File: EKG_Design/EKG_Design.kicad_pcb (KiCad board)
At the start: 2 copper layers, 40.7 x 23.2 mm, 55 parts, among them IC101 OPA2156IDGKR, IC102 OPA2156IDGKR, IC103 OPA2156IDGKR, IC104 INA826AIDR_/_SOIC8, J100 Conn_01x02_Pin, J101 Conn_01x02_Pin, J102 Conn_01x02_Pin, J103 Conn_01x02_Pin, J104 Conn_01x03_Pin, Q200 BC848C

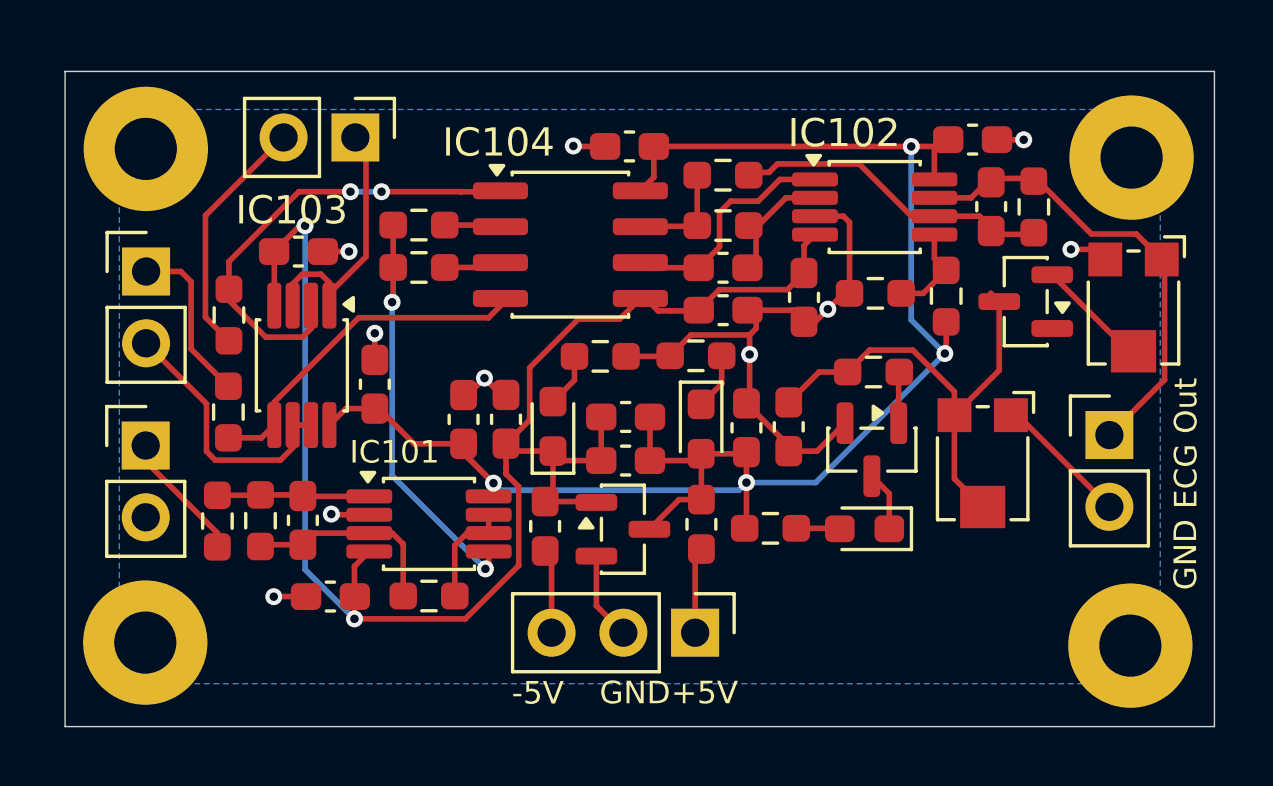
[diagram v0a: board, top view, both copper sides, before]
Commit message: Added GND zone to front of the board
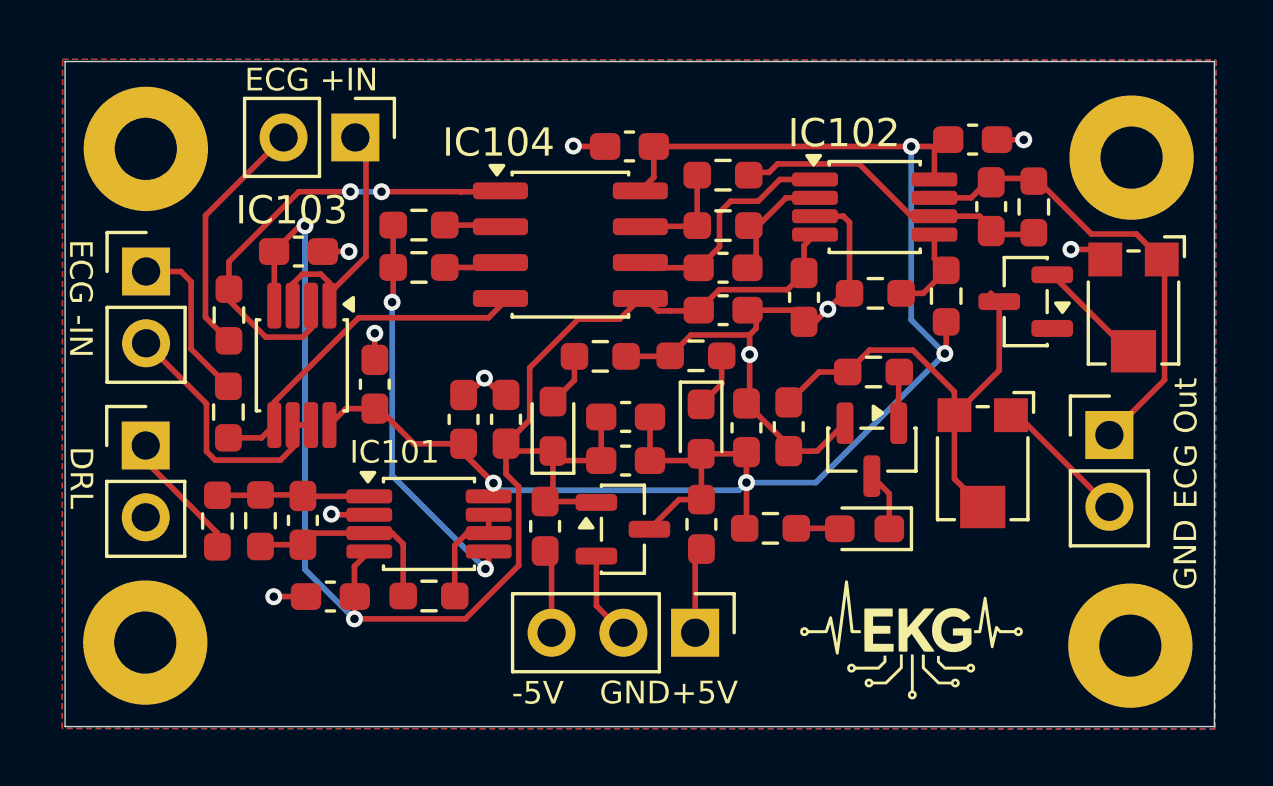
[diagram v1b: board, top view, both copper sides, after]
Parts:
- added G***: LOGO, logos:Logo, F.Cu at (122.0, 87.5)
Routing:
- added copper zone on F.Cu, net GND
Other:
- board size 40.7 x 23.2 mm -> 40.7 x 23.5 mm
- board text added: "DRL"
- board text added: "ECG +IN"
- board text added: "ECG -IN"

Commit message: added ibom and jobsets
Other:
- board text added: "T. Brown M. Mousa"
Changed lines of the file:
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@@
 			(drillshape 1)
 			(scaleselection 1)
-			(outputdirectory "")
+			(outputdirectory "Gerber")
 		)
 	)
@@
 		(sheetname "/ECG-PulseDetection/")
 		(sheetfile "ECG-PulseDetection.kicad_sch")
-		(units
-			(unit
-				(name "A")
-				(pins "1" "2")
-			)
-		)
 		(attr smd)
 		(duplicate_pad_numbers_are_jumpers no)
@@
 			(layer "F.CrtYd")
 		)
-		(fp_rect
-			(start -0.8 -0.4)
-			(end 0.8 0.4)
-			(stroke
-				(width 0.1)
-				(type solid)
-			)
-			(fill no)
-			(layer "F.Fab")
-		)
-		(fp_text user "${REFERENCE}"
-			(at 0 0 90)
-			(layer "F.Fab")
-			(effects
-				(font
-					(size 0.4 0.4)
-					(thickness 0.06)
-				)
-			)
-		)
 		(pad "1" smd roundrect
 			(at -0.8625 0 270)
@@
 	)
 	(gr_rect
-		(start 92.061217 66.883355)
-		(end 132.729689 90.41647)
+		(start 92.061217 66.892405)
+		(end 132.776931 90.41647)
 		(radius 2)
 		(stroke
@@
 		)
 	)
+	(gr_text "T. Brown\nM. Mousa"
+		(at 99.88025 89.853293 0)
+		(layer "F.SilkS")
+		(effects
+			(font
+				(size 0.8 0.8)
+				(thickness 0.1)
+			)
+			(justify left bottom)
+		)
+	)
 	(gr_text "-5V"
 		(at 107.867053 89.699214 0)
@@
 		)
 		(min_thickness 0.25)
-		(fill
+		(fill yes
 			(thermal_gap 0.5)
 			(thermal_bridge_width 0.5)
@@
 		(polygon
 			(pts
-				(xy 91.971622 66.805228) (xy 132.788244 66.830751) (xy 132.755605 90.502212) (xy 91.961602 90.484948)
+				(xy 93 68.5) (xy 131.487578 68.476705) (xy 131.5 89) (xy 93 89)
 			)
 		)
